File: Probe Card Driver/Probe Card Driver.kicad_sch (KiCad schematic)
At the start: 37 parts, among them J1 BNC, J10 FCR7350R, J11 FCR7350R, J12 LDO_SAMPLE, J13 MEMS_PINOUT, J14 Conn_01x03_Pin, J15 Conn_01x02_Pin, J2 Conn_01x03_Pin, J3 FCR7350R, J4 FCR7350R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

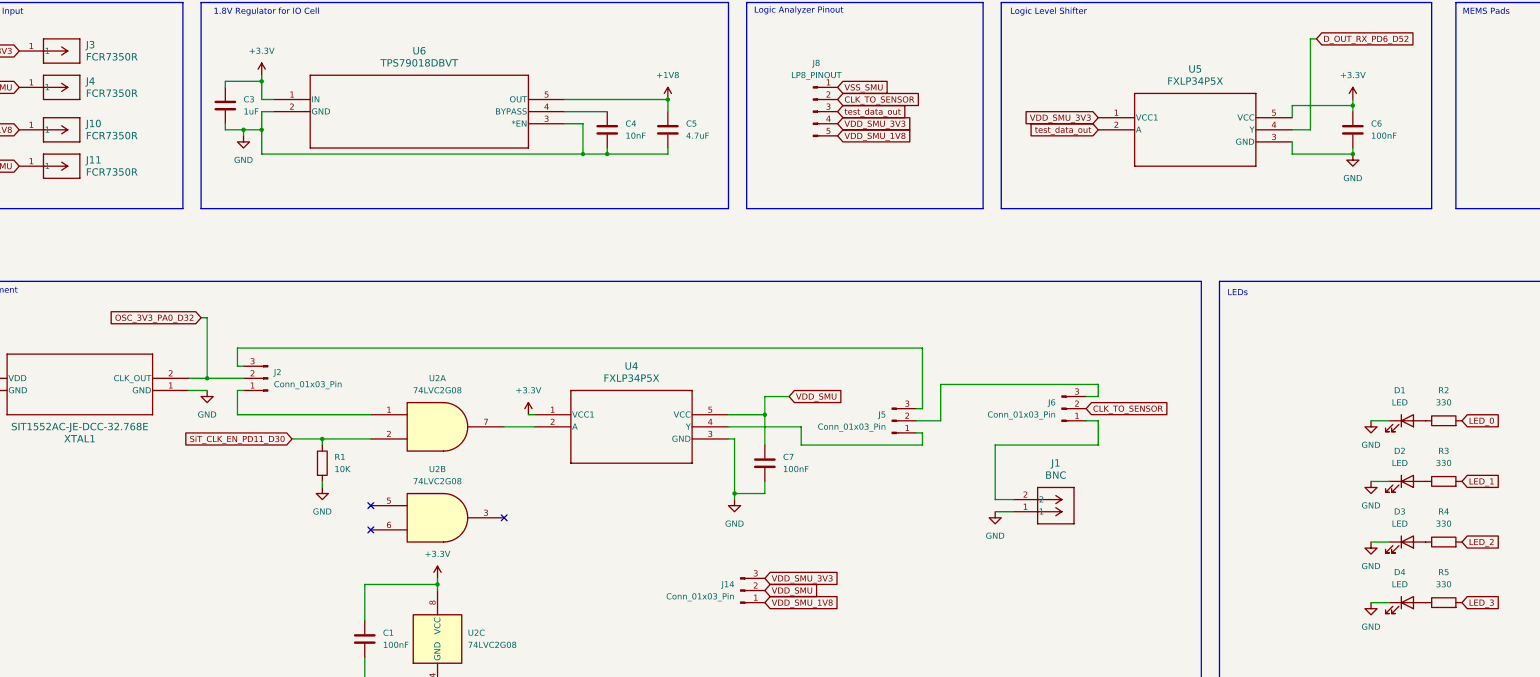
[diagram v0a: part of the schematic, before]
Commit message: Added BOM and Minor Updates
Added a BOM and included minor updates to layout and schematic.
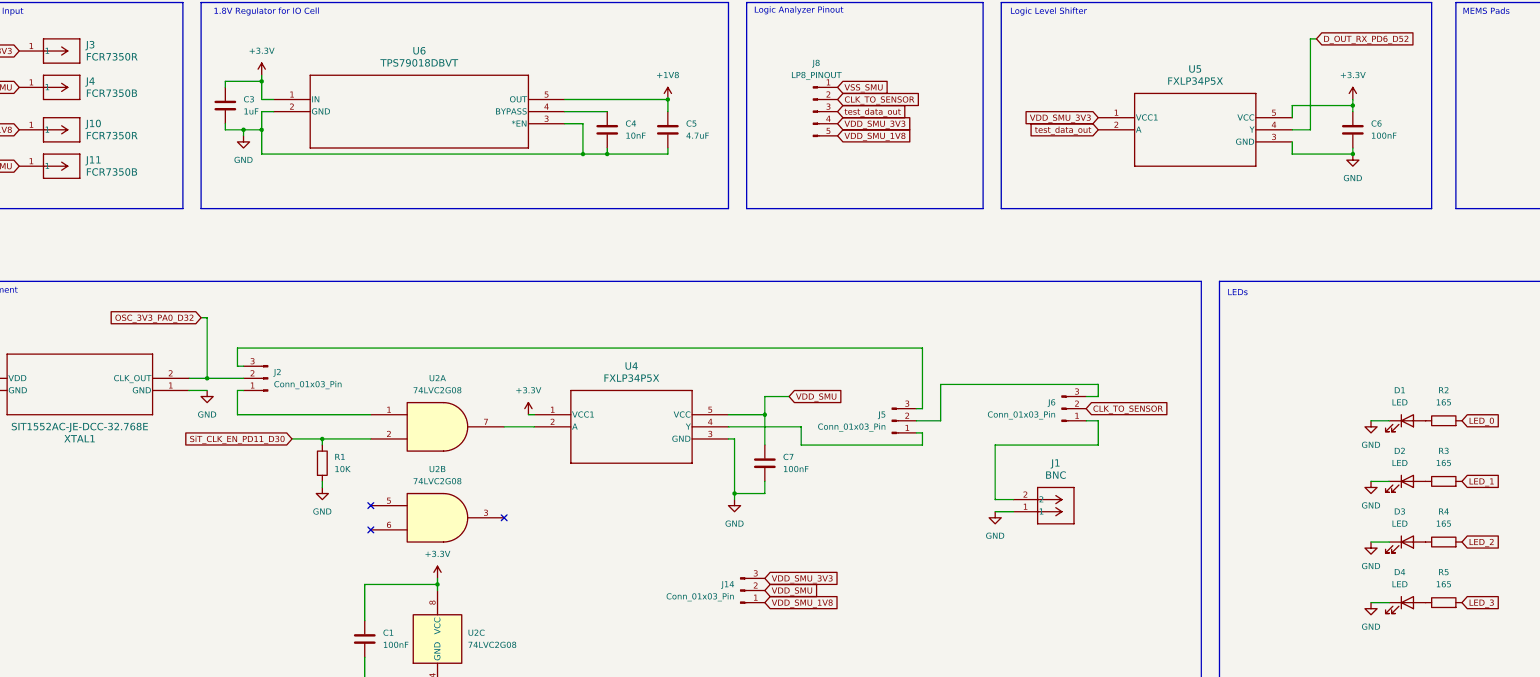
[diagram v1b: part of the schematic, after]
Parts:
- J11, J4: value FCR7350R -> FCR7350B
- R2, R3, R4, R5: value 330 -> 165
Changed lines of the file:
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@@
 			)
 		)
-		(property "Value" "FCR7350R"
+		(property "Value" "FCR7350B"
 			(at 76.2 218.4399 0)
 			(effects
@@
 			)
 		)
-		(property "Value" "FCR7350R"
+		(property "Value" "FCR7350B"
 			(at 76.2 234.9499 0)
 			(effects
@@
 			)
 		)
-		(property "Value" "330"
+		(property "Value" "165"
 			(at 360.68 295.91 90)
 			(effects
@@
 			)
 		)
-		(property "Value" "330"
+		(property "Value" "165"
 			(at 360.68 321.31 90)
 			(effects
@@
 			)
 		)
-		(property "Value" "330"
+		(property "Value" "165"
 			(at 360.68 308.61 90)
 			(effects
@@
 			)
 		)
-		(property "Value" "330"
+		(property "Value" "165"
 			(at 360.68 283.21 90)
 			(effects
